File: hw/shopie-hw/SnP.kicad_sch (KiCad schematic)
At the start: 4 parts, among them U5 ICM-20948

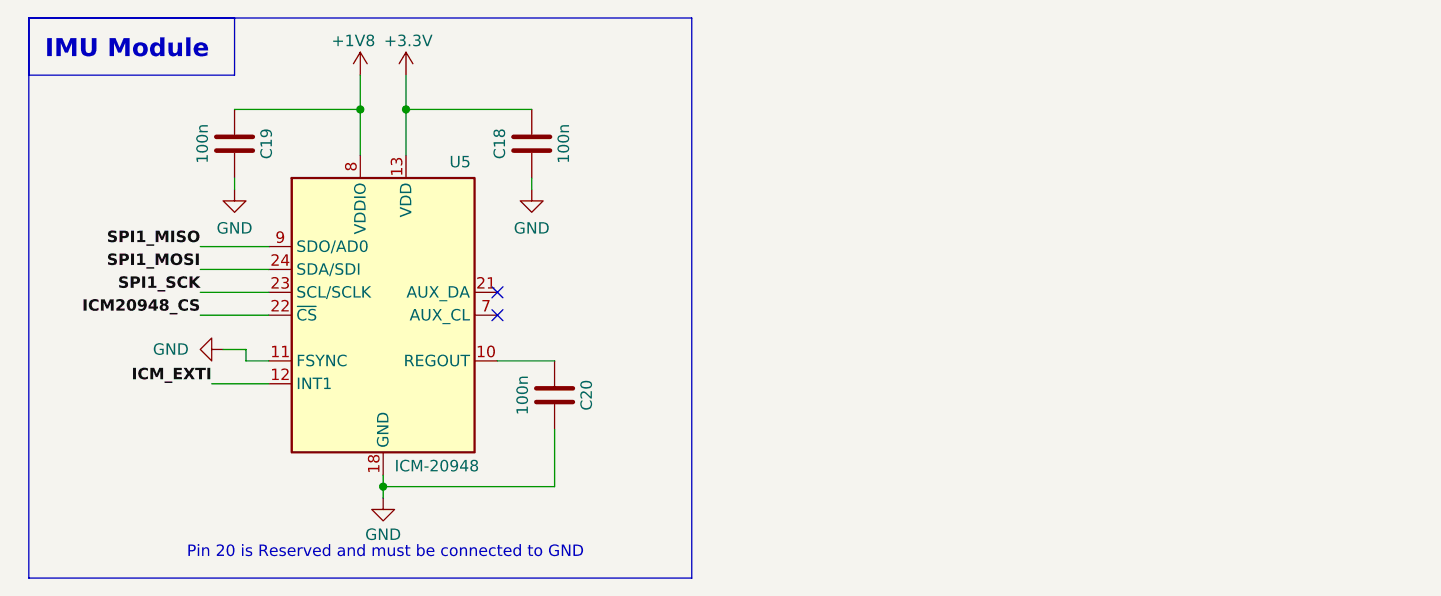
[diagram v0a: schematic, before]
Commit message: Update Barometer Symbol
- Adjustments to Barometer connections
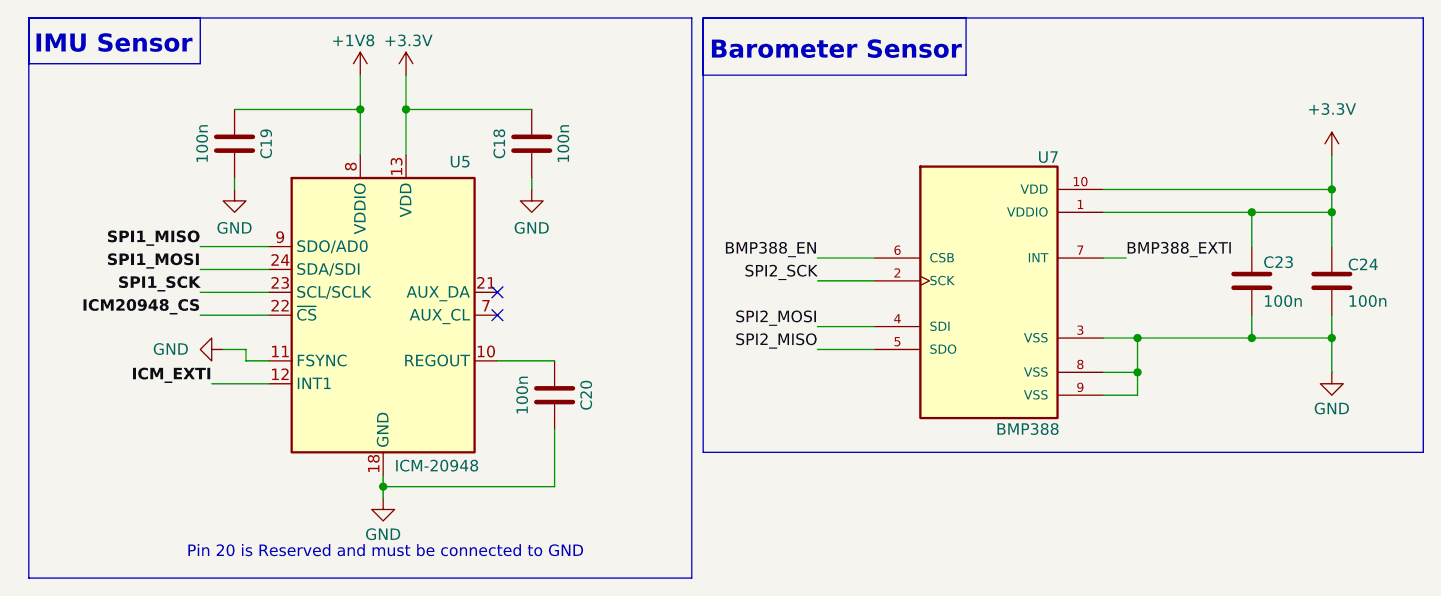
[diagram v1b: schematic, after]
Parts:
- added C23, C24: 100n, symbol Device:C
- added U7: BMP388, BMP388:PQFN50P200X200X80-10N, symbol shopie-hwLibrary:BMP388
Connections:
- net +3.3V: now also C23.1, C24.1, U7.1 (VDDIO), U7.10 (VDD)
- net GND: now also C23.2, C24.2, U7.3 (VSS), U7.8 (VSS), U7.9 (VSS)
- new net BMP388_EN: U7.6 (CSB)
- new net BMP388_EXTI: U7.7 (INT)
- new net SPI2_MISO: U7.5 (SDO)
- new net SPI2_MOSI: U7.4 (SDI)
- new net SPI2_SCK: U7.2 (SCK)
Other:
- note added: "Barometer Sensor"
- note added: "IMU Sensor"
- note removed: "IMU Module"

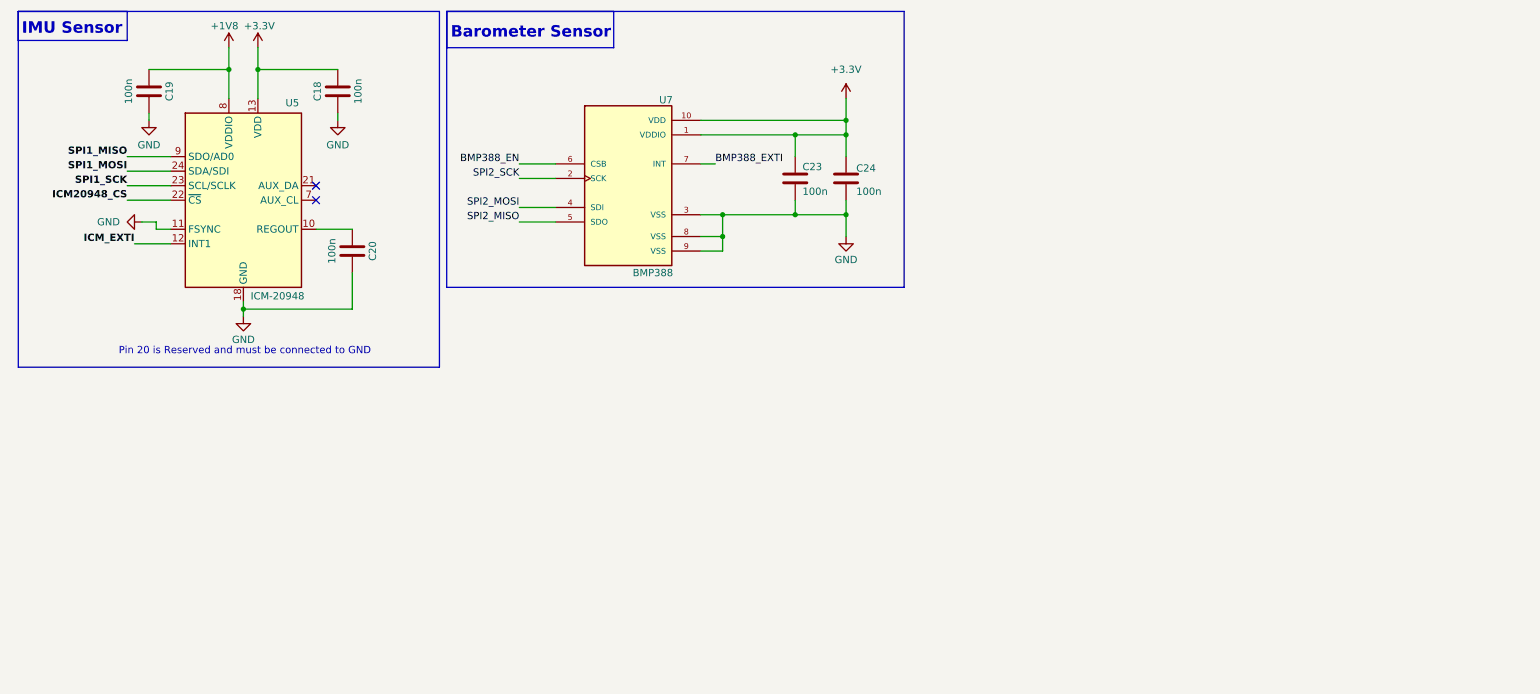
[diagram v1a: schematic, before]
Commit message: Add TMF8801 ToF Sensor
- Added TMF8801 ToF sensor symbol to schematic (SnP Sheet)
- Connected TMF8801 to STM32 MCU via I2C (SCL, SDA) and INT to EXTI-GPIO
- Connected EN pin to MCU
- Added 100nF decoupling capacitors to VDD, VDDC and VDDV as per datasheet recommendation
- Included pull-up resistors to 1.8V on SDA, SCL, and INT lines
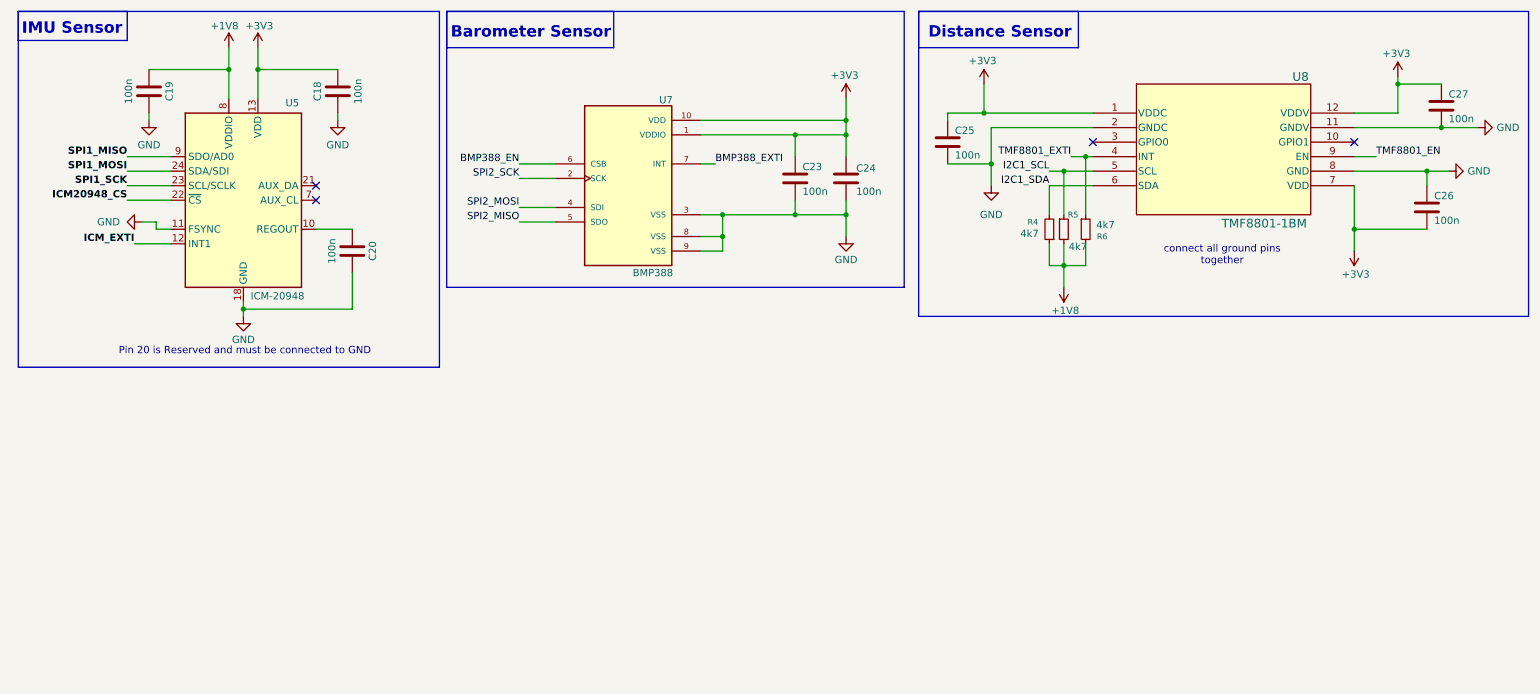
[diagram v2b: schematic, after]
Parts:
- added C25, C26, C27: 100n, symbol Device:C
- added R4, R5, R6: 4k7, symbol Device:R_Small
- added U8: TMF8801-1BM, TMF8801-1BM_AMS, symbol shopie-hwLibrary:TMF8801-1BM
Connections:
- net +1V8: now also R4.1, R5.2, R6.2
- net GND: now also C25.2, C26.1, C27.2, U8.11 (GNDV), U8.2 (GNDC), U8.8 (GND)
- net +3.3V renamed +3V3
- net +3V3: now also C25.1, C26.2, C27.1, U8.1 (VDDC), U8.12 (VDDV), U8.7 (VDD)
- new net I2C1_SCL: R5.1, U8.5 (SCL)
- new net I2C1_SDA: R4.2, U8.6 (SDA)
- new net TMF8801_EN: U8.9 (EN)
- new net TMF8801_EXTI: R6.1, U8.4 (INT)
- no-connect marks 2 -> 4
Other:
- note added: "Distance Sensor"
- note added: "connect all ground pins together"

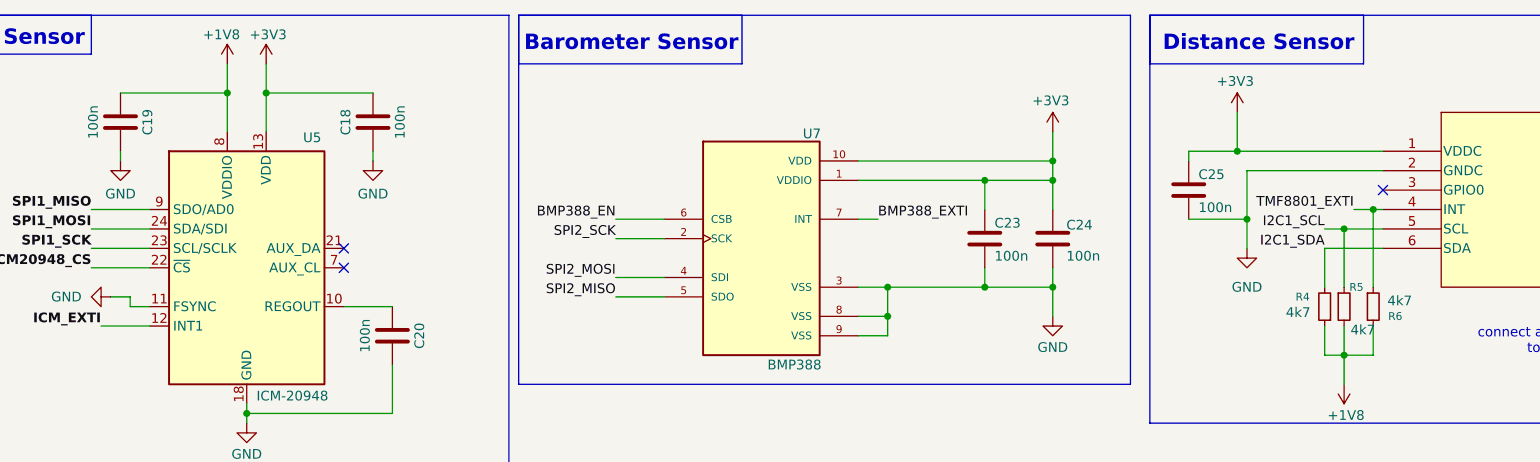
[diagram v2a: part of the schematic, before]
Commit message: Add ESP32 module to schematic and STM32 IOC pinout
- Added ESP32 (Arduino Nano ESP32 WROOM32) module symbol and footprint to the schematic
- Connected communication lines (UART/SPI/I2C as planned) between ESP32 and STM32 MCU
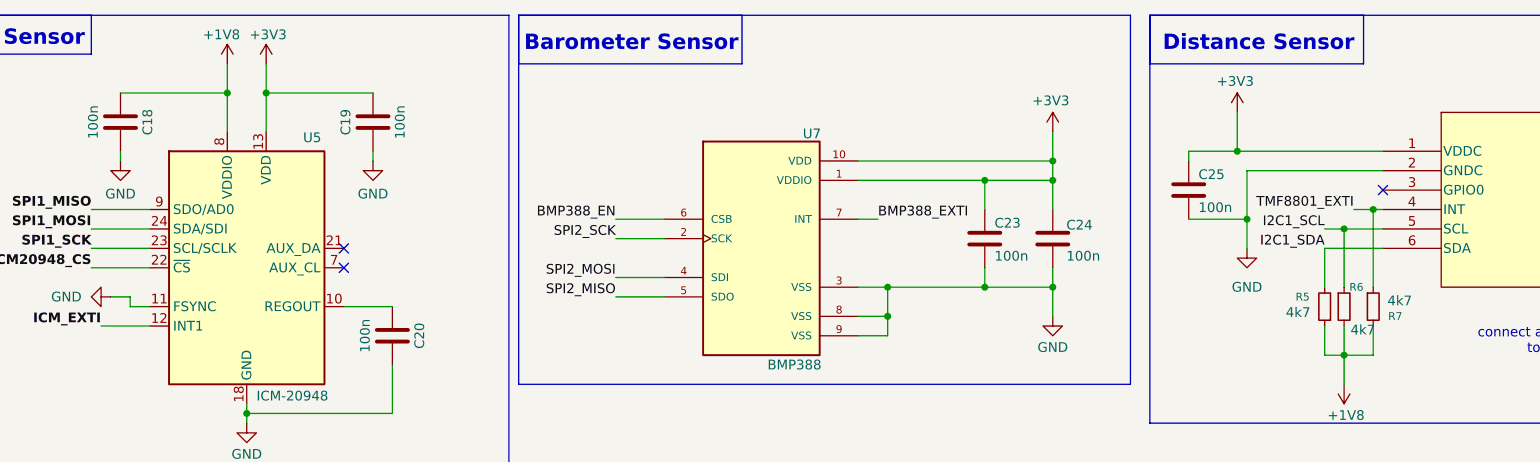
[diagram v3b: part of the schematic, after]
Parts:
- renumbered C19 to C18, C18 to C19, R4 to R5, R5 to R6, R6 to R7

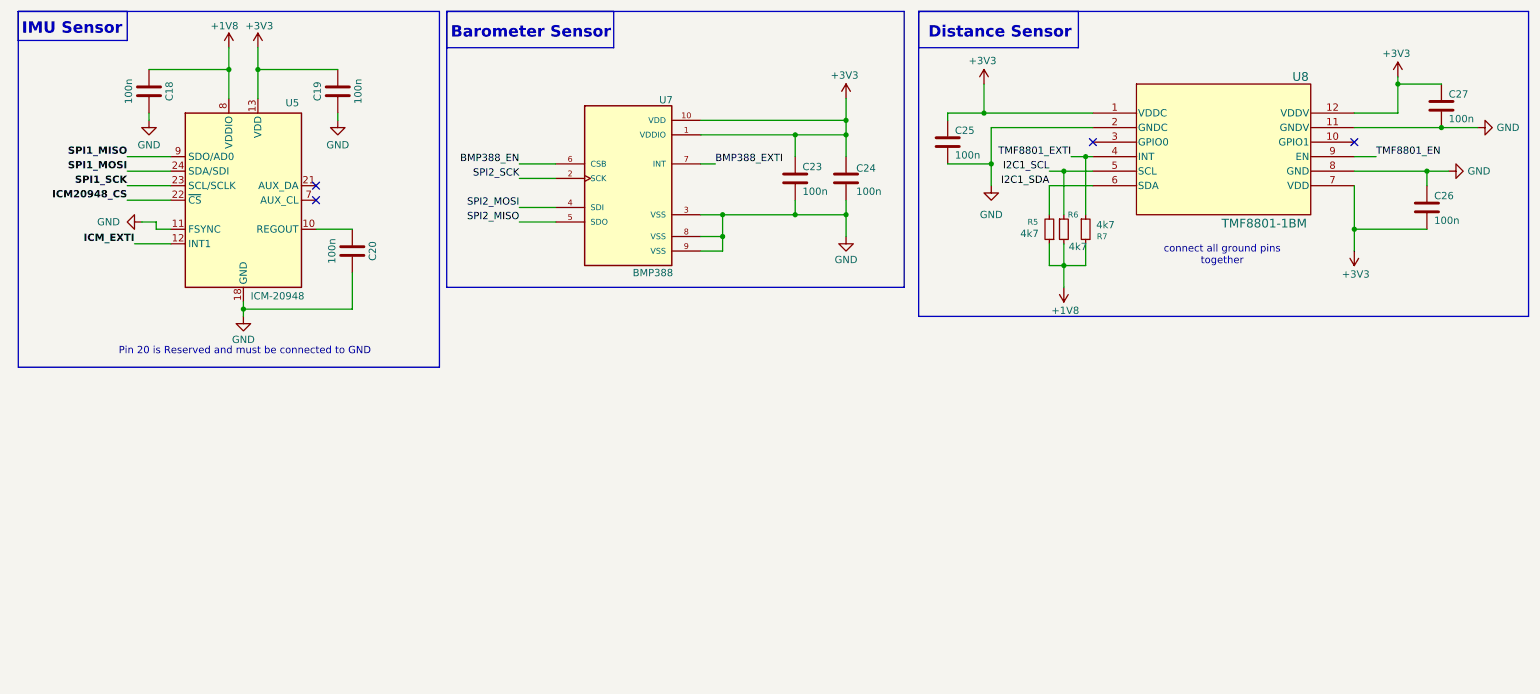
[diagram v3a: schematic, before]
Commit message: Add LTC2943 battery fuel gauge
- Added LTC2943 current and voltage monitor IC to the schematic
- Connected LTC2943 SENSE+ and SENSE− pins to the 0.5mΩ, 9W shunt resistor terminals for current sensing
- Shunt resistor placed in high-side battery+ line for accurate current measurement
- Added I2C connections (SDA, SCL) to MCU
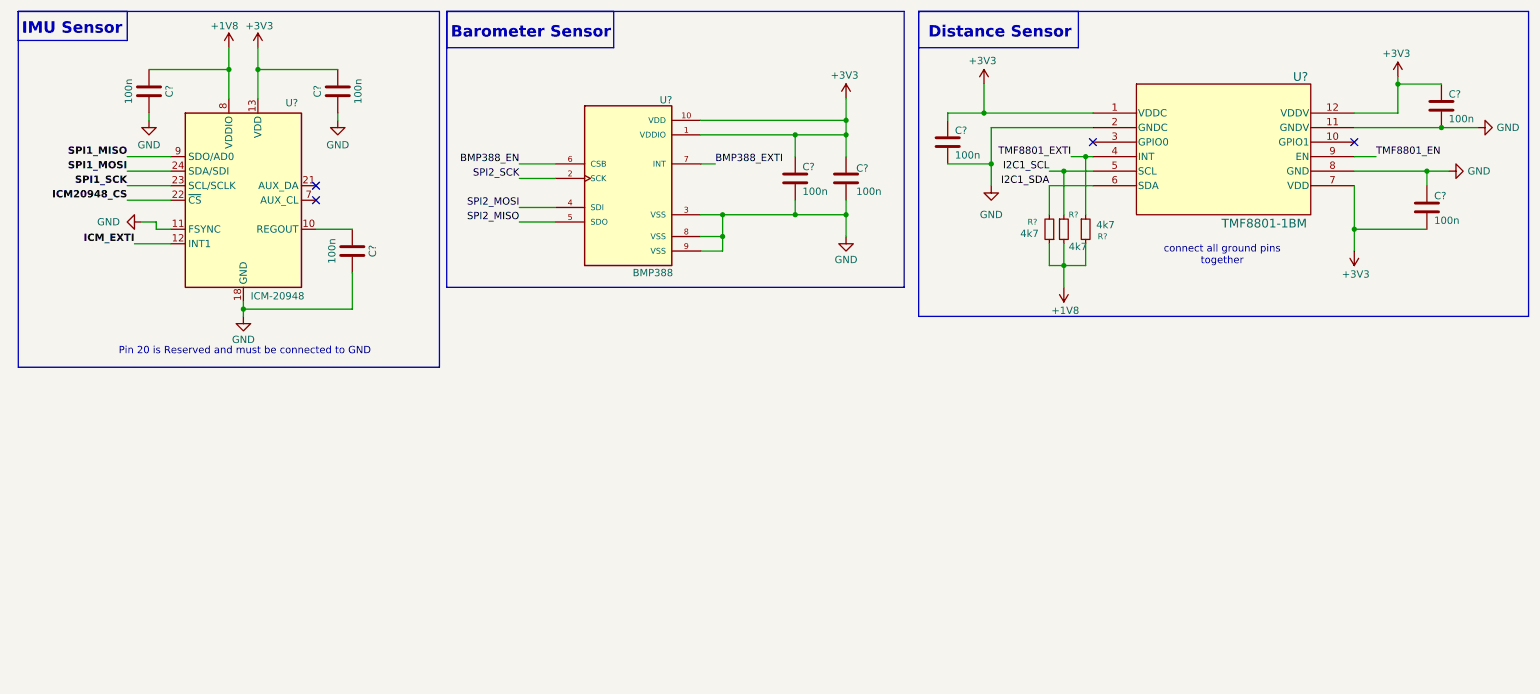
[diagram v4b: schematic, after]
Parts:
- renumbered C26 to C?, C18 to C?, C20 to C?, C27 to C?, C19 to C?, C23 to C?, C25 to C?, C24 to C?, R6 to R?, R5 to R?, R7 to R?, U7 to U?, U8 to U?, U5 to U?

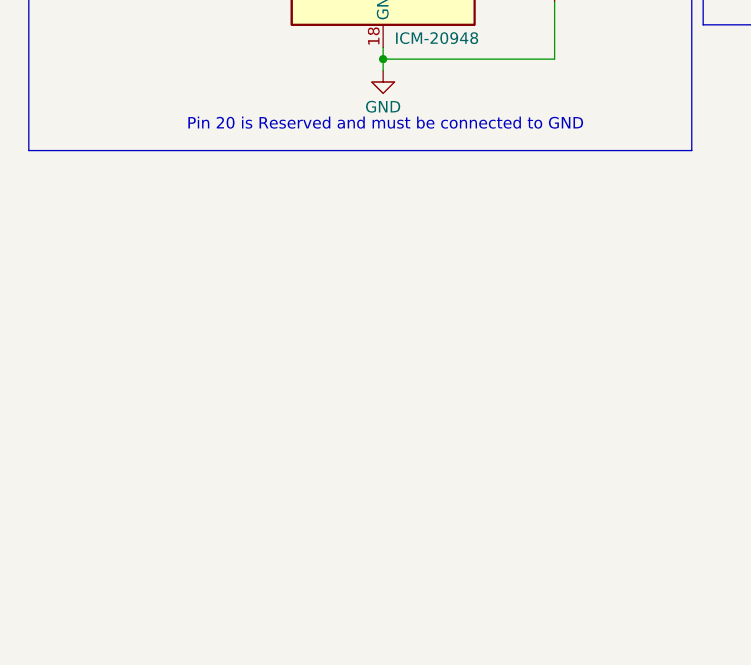
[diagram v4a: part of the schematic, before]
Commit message: Add ESC symbol and complete schematic connections, Update MCU pinout
- Created custom KiCad symbol for the HAKRC BLHeli_32 40A 4-in-1 ESC
- Connected ESC signal lines to MCU PWM outputs, CURR to ADC, and TX to UART RX
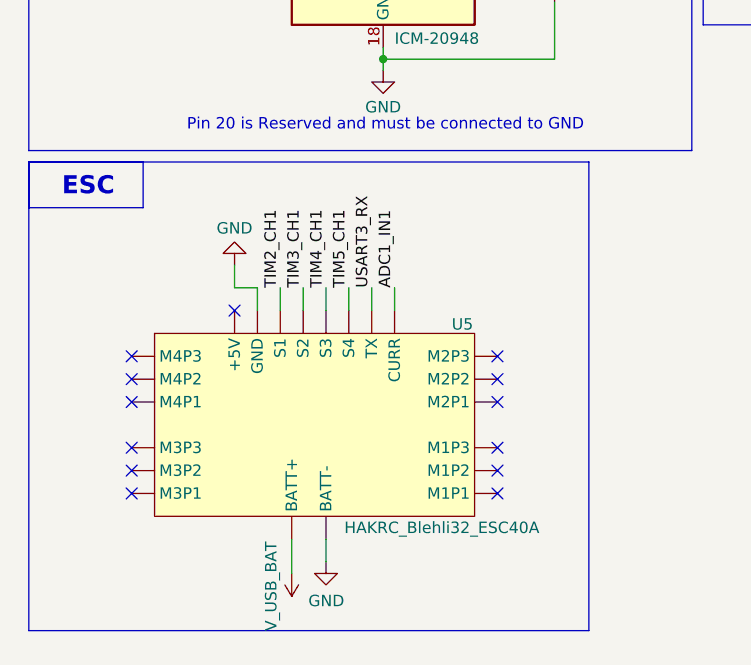
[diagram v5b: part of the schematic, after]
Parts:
- added U5: HAKRC_Blehli32_ESC40A, symbol shopie-hwLibrary:HAKRC_Blehli32_ESC40A
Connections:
- net GND: now also U5. (M1P1)
- new net ADC1_IN1: U5. (M1P1)
- new net TIM2_CH1: U5. (M1P1)
- new net TIM3_CH1: U5. (M1P1)
- new net TIM4_CH1: U5. (M1P1)
- new net TIM5_CH1: U5. (M1P1)
- new net USART3_RX: U5. (M1P1)
- new net V_USB_BAT: U5. (M1P1)
- no-connect marks 4 -> 17
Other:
- note added: "ESC"
